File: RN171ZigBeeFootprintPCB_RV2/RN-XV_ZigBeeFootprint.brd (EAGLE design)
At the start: 39.1 x 52.1 mm, 20 parts

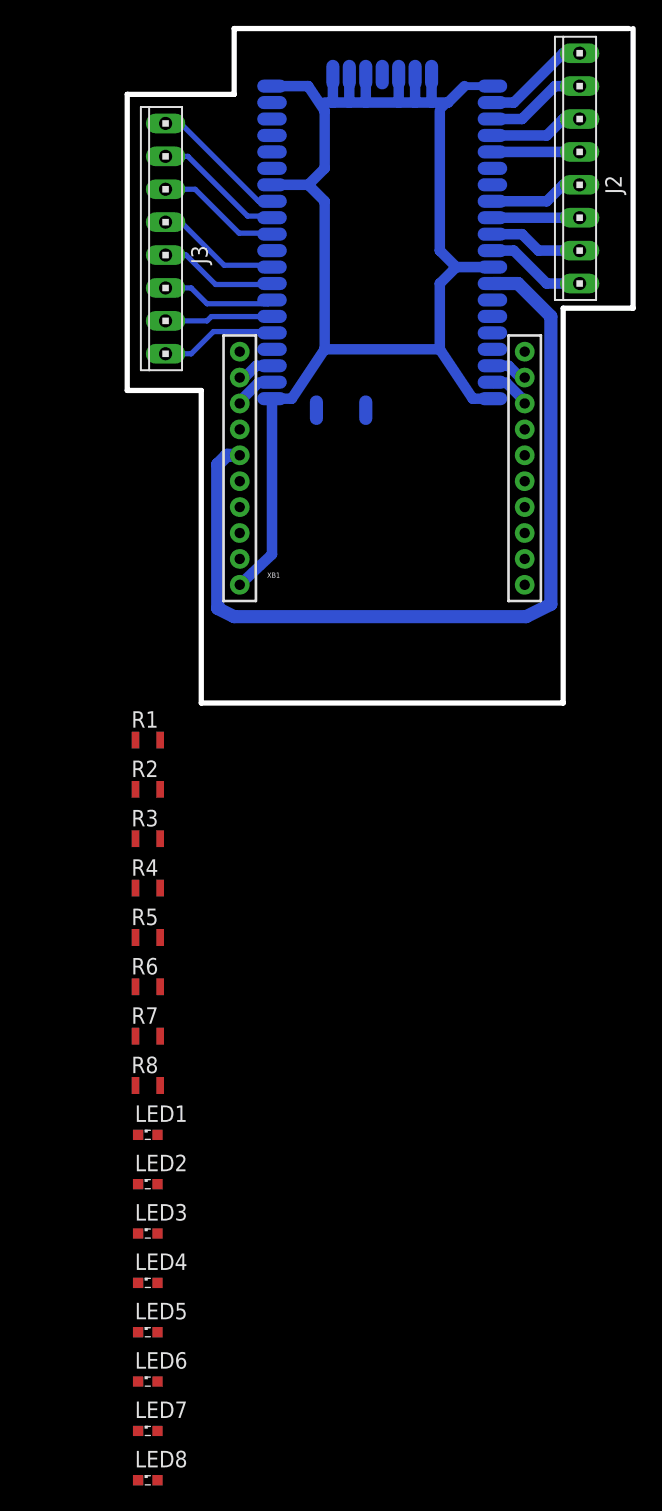
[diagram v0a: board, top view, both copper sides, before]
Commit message: Wired LED in to the PCB design.
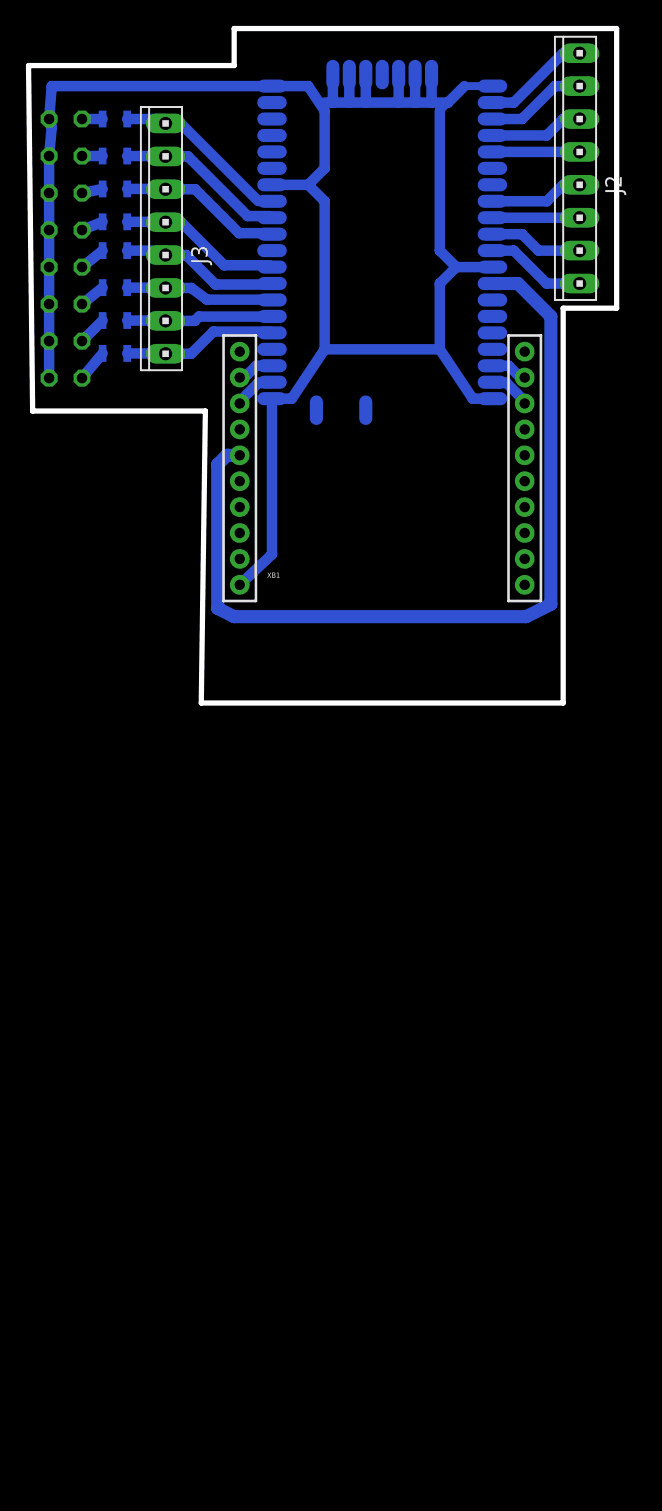
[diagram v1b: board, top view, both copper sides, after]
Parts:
- LED1, LED2, LED3, LED4, LED5, LED6, LED7, LED8: device eagle-ltspice:LED_SML0603 -> eagle-ltspice:LED_LD260
- moved LED8 105.3 mm to (-10.5, 39.7), flipped to the bottom
- moved LED7 98.6 mm to (-10.5, 36.8), flipped to the bottom
- moved LED6 92.0 mm to (-10.5, 34.0), flipped to the bottom
- moved LED5 85.3 mm to (-10.5, 31.1), flipped to the bottom
- moved LED4 78.7 mm to (-10.5, 28.3), flipped to the bottom
- moved R8 74.7 mm to (-6.67, 39.7), flipped to the bottom, turned to 180 degrees
- moved LED3 72.0 mm to (-10.5, 25.4), flipped to the bottom
- moved R7 68.0 mm to (-6.67, 36.8), flipped to the bottom, turned to 180 degrees
- moved LED2 65.4 mm to (-10.5, 22.5), flipped to the bottom
- moved R6 61.6 mm to (-6.67, 34.3), flipped to the bottom, turned to 180 degrees
- moved LED1 58.8 mm to (-10.5, 19.7), flipped to the bottom
- moved R5 55.3 mm to (-6.67, 31.8), flipped to the bottom, turned to 180 degrees
- moved R4 49.3 mm to (-6.67, 29.5), flipped to the bottom, turned to 180 degrees
- moved R3 42.6 mm to (-6.67, 26.7), flipped to the bottom, turned to 180 degrees
- moved R2 36.3 mm to (-6.67, 24.1), flipped to the bottom, turned to 180 degrees
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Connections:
- removed net N$12: J1.13, J3.1
- removed net N$13: J1.12, J3.2
- removed net N$14: J1.11, J3.3
- removed net N$15: J1.9, J3.4
- removed net N$16: J1.8, J3.5
- removed net N$17: J1.7, J3.6
- removed net N$18: J1.6, J3.7
- removed net N$19: J1.5, J3.8
- net GND: now also LED1.K, LED2.K, LED3.K, LED4.K, LED5.K, LED6.K, LED7.K, LED8.K; no longer LED1.C, LED2.C, LED3.C, LED4.C, LED5.C, LED6.C, LED7.C, LED8.C
- net N$30: now also J1.5, J3.8
- net N$31: now also J1.6, J3.7
- net N$32: now also J1.7, J3.6
- net N$33: now also J1.8, J3.5
- net N$34: now also J1.9, J3.4
- net N$35: now also J1.11, J3.3
- net N$36: now also J1.12, J3.2
- net N$37: now also J1.13, J3.1
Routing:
- net GND: track 114.1 -> 153.7 mm
- net N$37: track 0.00 -> 14.0 mm
- net N$36: track 0.00 -> 13.2 mm
- net N$35: track 0.00 -> 12.6 mm
- net N$34: track 0.00 -> 12.6 mm
- net N$33: track 0.00 -> 12.5 mm
- net N$30: track 0.00 -> 12.0 mm
- net N$32: track 0.00 -> 11.5 mm
- net N$31: track 0.00 -> 11.3 mm
- net N$12: track 10.7 -> 0.00 mm
- net N$13: track 10.2 -> 0.00 mm
- net N$14: track 9.65 -> 0.00 mm
- net N$15: track 9.65 -> 0.00 mm
- net N$16: track 9.19 -> 0.00 mm
- net N$19: track 8.97 -> 0.00 mm
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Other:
- board size 39.1 x 52.1 mm -> 45.4 x 52.1 mm
- board text added: "REV2.0"

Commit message: Connecting voltage supply to all components.
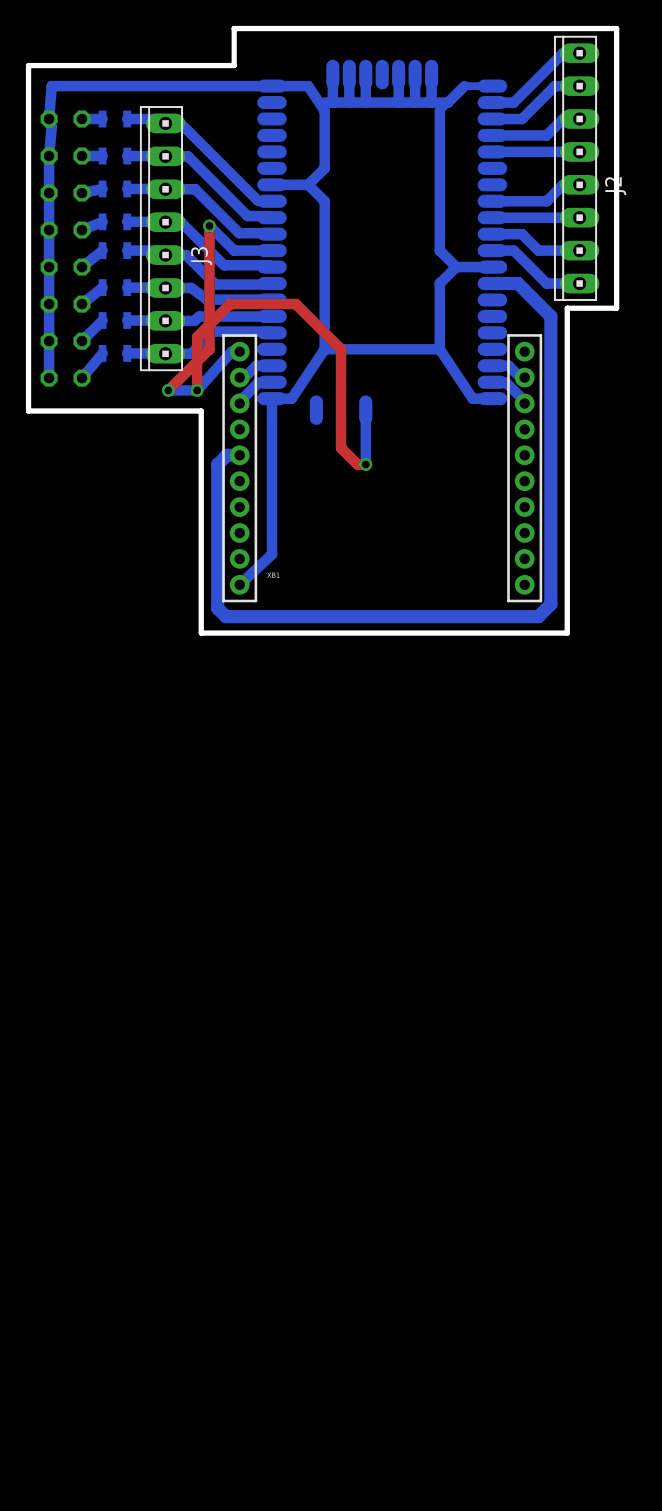
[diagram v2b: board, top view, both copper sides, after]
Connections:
- removed net VCC: XB1.1
- net VDD_3.3V: now also J1.49, XB1.1
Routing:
- net VDD_3.3V: track 0.00 -> 58.5 mm, vias 0 -> 4
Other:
- board size 45.4 x 52.1 mm -> 45.4 x 46.7 mm
- board text added: "GND"
- board text added: "REV 2.0"
- board text removed: "REV2.0"
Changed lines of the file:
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@@
 <layer number="36" name="bGlue" color="7" fill="5" visible="no" active="yes"/>
 <layer number="37" name="tTest" color="7" fill="1" visible="no" active="yes"/>
-<layer number="38" name="bTest" color="7" fill="1" visible="no" active="yes"/>
+<layer number="38" name="bTest" color="7" fill="1" visible="yes" active="yes"/>
 <layer number="39" name="tKeepout" color="4" fill="11" visible="yes" active="yes"/>
 <layer number="40" name="bKeepout" color="1" fill="11" visible="yes" active="yes"/>
@@
 <board>
 <plain>
-<wire x1="-13.335" y1="43.815" x2="-13.0175" y2="17.145" width="0.4064" layer="46"/>
-<wire x1="-13.0175" y1="17.145" x2="0.3175" y2="17.145" width="0.4064" layer="46"/>
-<wire x1="0.3175" y1="17.145" x2="0" y2="-5.3975" width="0.4064" layer="46"/>
-<wire x1="0" y1="-5.3975" x2="27.94" y2="-5.3975" width="0.4064" layer="46"/>
-<wire x1="27.94" y1="-5.3975" x2="27.94" y2="25.0825" width="0.4064" layer="46"/>
-<wire x1="27.94" y1="25.0825" x2="32.0675" y2="25.0825" width="0.4064" layer="46"/>
+<wire x1="-13.335" y1="43.815" x2="-13.335" y2="17.145" width="0.4064" layer="46"/>
+<wire x1="-13.335" y1="17.145" x2="0" y2="17.145" width="0.4064" layer="46"/>
+<wire x1="0" y1="17.145" x2="0" y2="0" width="0.4064" layer="46"/>
+<wire x1="0" y1="0" x2="28.2575" y2="0" width="0.4064" layer="46"/>
+<wire x1="28.2575" y1="0" x2="28.2575" y2="25.0825" width="0.4064" layer="46"/>
+<wire x1="28.2575" y1="25.0825" x2="32.0675" y2="25.0825" width="0.4064" layer="46"/>
 <wire x1="32.0675" y1="25.0825" x2="32.0675" y2="46.6725" width="0.4064" layer="46"/>
 <wire x1="32.0675" y1="46.6725" x2="2.54" y2="46.6725" width="0.4064" layer="46"/>
 <wire x1="2.54" y1="46.6725" x2="2.54" y2="43.815" width="0.4064" layer="46"/>
 <wire x1="2.54" y1="43.815" x2="-13.335" y2="43.815" width="0.4064" layer="46"/>
-<text x="17.4625" y="-3.81" size="1.778" layer="48">REV2.0</text>
+<text x="9.8425" y="2.8575" size="1.778" layer="48">REV 2.0</text>
+<text x="16.51" y="38.1" size="1.778" layer="38" rot="MR0">GND</text>
+<text x="12.065" y="28.8925" size="1.778" layer="38" rot="MR270">GND</text>
+<text x="15.875" y="28.575" size="1.778" layer="38" rot="MR90">GND</text>
 </plain>
 <attributes>
@@
 <wire x1="1.9797" y1="13.7272" x2="1.27" y2="13.0175" width="1.016" layer="16"/>
 <wire x1="1.27" y1="13.0175" x2="1.27" y2="1.905" width="1.016" layer="16"/>
-<wire x1="1.27" y1="1.905" x2="2.54" y2="1.27" width="1.016" layer="16"/>
-<wire x1="2.54" y1="1.27" x2="25.0825" y2="1.27" width="1.016" layer="16"/>
-<wire x1="25.0825" y1="1.27" x2="26.9875" y2="2.2225" width="1.016" layer="16"/>
+<wire x1="1.27" y1="1.905" x2="1.905" y2="1.27" width="1.016" layer="16"/>
+<wire x1="1.905" y1="1.27" x2="26.035" y2="1.27" width="1.016" layer="16"/>
+<wire x1="26.035" y1="1.27" x2="26.9875" y2="2.2225" width="1.016" layer="16"/>
 <wire x1="26.9875" y1="2.2225" x2="26.9875" y2="24.4475" width="1.016" layer="16"/>
 <wire x1="26.9875" y1="24.4475" x2="24.4475" y2="26.9875" width="1.016" layer="16"/>
@@
 <wire x1="2.97" y1="17.8798" x2="2.97" y2="17.7272" width="0.8128" layer="16"/>
 </signal>
-<signal name="VCC">
-<contactref element="XB1" pad="1"/>
-</signal>
 <signal name="VDD_3.3V">
 <contactref element="J1" pad="10"/>
+<contactref element="J1" pad="49"/>
+<contactref element="XB1" pad="1"/>
+<wire x1="2.97" y1="21.7272" x2="2.3597" y2="21.7272" width="0.8128" layer="16"/>
+<wire x1="2.3597" y1="21.7272" x2="-0.3175" y2="18.7325" width="0.8128" layer="16"/>
+<via x="-0.3175" y="18.7325" extent="1-16" drill="0.6" shape="square"/>
+<wire x1="-0.3175" y1="18.7325" x2="-0.3175" y2="22.86" width="0.8128" layer="1"/>
+<wire x1="-0.3175" y1="22.86" x2="2.2225" y2="25.4" width="0.8128" layer="1"/>
+<wire x1="2.2225" y1="25.4" x2="7.3025" y2="25.4" width="0.8128" layer="1"/>
+<wire x1="7.3025" y1="25.4" x2="10.795" y2="21.9075" width="0.8128" layer="1"/>
+<wire x1="10.795" y1="21.9075" x2="10.795" y2="14.2875" width="0.8128" layer="1"/>
+<wire x1="10.795" y1="14.2875" x2="12.065" y2="13.0175" width="0.8128" layer="1"/>
+<wire x1="12.065" y1="13.0175" x2="12.7" y2="13.0175" width="0.8128" layer="1"/>
+<via x="12.7" y="13.0175" extent="1-16" drill="0.6" shape="square"/>
+<wire x1="12.7" y1="13.0175" x2="12.7" y2="17.2085" width="0.8128" layer="16"/>
+<wire x1="5.461" y1="29.5275" x2="2.54" y2="29.5275" width="0.8128" layer="16"/>
+<wire x1="2.54" y1="29.5275" x2="0.635" y2="31.4325" width="0.8128" layer="16"/>
+<via x="0.635" y="31.4325" extent="1-16" drill="0.6" shape="square"/>
+<wire x1="0.635" y1="31.4325" x2="0.635" y2="21.9075" width="0.8128" layer="1"/>
+<wire x1="0.635" y1="21.9075" x2="-2.54" y2="18.7325" width="0.8128" layer="1"/>
+<via x="-2.54" y="18.7325" extent="1-16" drill="0.6" shape="square"/>
+<wire x1="-2.54" y1="18.7325" x2="-0.3175" y2="18.7325" width="0.8128" layer="16"/>
 </signal>
 <signal name="N$1">

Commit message: Connecting RN171's 34 pin to VCC
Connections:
- net VDD_3.3V: now also J1.34
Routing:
- net VDD_3.3V: track 58.5 -> 98.2 mm, vias 4 -> 6
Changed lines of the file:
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@@
 <via x="-2.54" y="18.7325" extent="1-16" drill="0.6" shape="square"/>
 <wire x1="-2.54" y1="18.7325" x2="-0.3175" y2="18.7325" width="0.8128" layer="16"/>
+<contactref element="J1" pad="34"/>
+<wire x1="22.479" y1="34.6075" x2="25.7175" y2="34.6075" width="0.8128" layer="16"/>
+<wire x1="25.7175" y1="34.6075" x2="25.7175" y2="35.56" width="0.8128" layer="16"/>
+<via x="25.7175" y="35.56" extent="1-16" drill="0.6" shape="square"/>
+<wire x1="25.7175" y1="35.56" x2="15.875" y2="35.56" width="0.8128" layer="1"/>
+<wire x1="15.875" y1="35.56" x2="15.875" y2="13.0175" width="0.8128" layer="1"/>
+<via x="15.875" y="13.0175" extent="1-16" drill="0.6" shape="square"/>
+<wire x1="15.875" y1="13.0175" x2="12.7" y2="13.0175" width="0.8128" layer="16"/>
 </signal>
 <signal name="N$1">

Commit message: Replace one of the line in the PCB design.
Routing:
- net VDD_3.3V: track 98.2 -> 92.8 mm, vias 6 -> 4
- net GND: track 153.7 -> 155.0 mm
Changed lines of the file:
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@@
 <wire x1="22.479" y1="28.2575" x2="19.685" y2="28.2575" width="0.8128" layer="16"/>
 <wire x1="19.685" y1="28.2575" x2="18.415" y2="26.9875" width="0.8128" layer="16"/>
-<wire x1="18.415" y1="26.9875" x2="18.415" y2="21.9075" width="0.8128" layer="16"/>
-<wire x1="18.415" y1="21.9075" x2="20.955" y2="18.0975" width="0.8128" layer="16"/>
+<wire x1="18.415" y1="26.9875" x2="18.415" y2="20.6375" width="0.8128" layer="16"/>
 <wire x1="20.955" y1="18.0975" x2="22.479" y2="18.0975" width="0.8128" layer="16"/>
 <contactref element="J1" pad="27"/>
@@
 <wire x1="16.51" y1="43.1165" x2="16.51" y2="40.9575" width="0.8128" layer="16"/>
 <wire x1="17.78" y1="43.1165" x2="17.78" y2="40.9575" width="0.8128" layer="16"/>
-<wire x1="18.415" y1="21.9075" x2="9.525" y2="21.9075" width="0.8128" layer="16"/>
-<wire x1="9.525" y1="21.9075" x2="6.985" y2="18.0975" width="0.8128" layer="16"/>
 <wire x1="6.985" y1="18.0975" x2="5.461" y2="18.0975" width="0.8128" layer="16"/>
-<wire x1="8.255" y1="34.6075" x2="9.525" y2="33.3375" width="0.8128" layer="16"/>
-<wire x1="9.525" y1="33.3375" x2="9.525" y2="21.9075" width="0.8128" layer="16"/>
+<wire x1="8.255" y1="34.6075" x2="9.525" y2="33.3375" width="0" layer="19" extent="1-16"/>
+<wire x1="9.525" y1="33.3375" x2="9.525" y2="21.9075" width="0" layer="19" extent="1-16"/>
 <wire x1="2.97" y1="3.7272" x2="5.461" y2="6.0785" width="0.8128" layer="16"/>
 <contactref element="LED8" pad="K"/>
@@
 <wire x1="5.461" y1="42.2275" x2="-11.545" y2="42.2275" width="0.8128" layer="16"/>
 <wire x1="-11.545" y1="42.2275" x2="-11.7475" y2="39.6875" width="0.8128" layer="16"/>
+<wire x1="6.985" y1="18.0975" x2="6.985" y2="11.43" width="0.8128" layer="16"/>
+<wire x1="6.985" y1="11.43" x2="7.9375" y2="10.795" width="0.8128" layer="16"/>
+<wire x1="7.9375" y1="10.795" x2="20.0025" y2="10.795" width="0.8128" layer="16"/>
+<wire x1="20.0025" y1="10.795" x2="20.955" y2="11.43" width="0.8128" layer="16"/>
+<wire x1="20.955" y1="11.43" x2="20.955" y2="18.0975" width="0.8128" layer="16"/>
+<wire x1="18.415" y1="20.6375" x2="20.955" y2="18.0975" width="0.8128" layer="16"/>
 </signal>
 <signal name="RX">
@@
 <via x="12.7" y="13.0175" extent="1-16" drill="0.6" shape="square"/>
 <wire x1="12.7" y1="13.0175" x2="12.7" y2="17.2085" width="0.8128" layer="16"/>
-<wire x1="5.461" y1="29.5275" x2="2.54" y2="29.5275" width="0.8128" layer="16"/>
-<wire x1="2.54" y1="29.5275" x2="0.635" y2="31.4325" width="0.8128" layer="16"/>
-<via x="0.635" y="31.4325" extent="1-16" drill="0.6" shape="square"/>
-<wire x1="0.635" y1="31.4325" x2="0.635" y2="21.9075" width="0.8128" layer="1"/>
-<wire x1="0.635" y1="21.9075" x2="-2.54" y2="18.7325" width="0.8128" layer="1"/>
-<via x="-2.54" y="18.7325" extent="1-16" drill="0.6" shape="square"/>
-<wire x1="-2.54" y1="18.7325" x2="-0.3175" y2="18.7325" width="0.8128" layer="16"/>
 <contactref element="J1" pad="34"/>
 <wire x1="22.479" y1="34.6075" x2="25.7175" y2="34.6075" width="0.8128" layer="16"/>
@@
 <via x="15.875" y="13.0175" extent="1-16" drill="0.6" shape="square"/>
 <wire x1="15.875" y1="13.0175" x2="12.7" y2="13.0175" width="0.8128" layer="16"/>
+<wire x1="5.461" y1="29.5275" x2="7.3025" y2="29.5275" width="0.8128" layer="16"/>
+<wire x1="7.3025" y1="29.5275" x2="12.7" y2="24.13" width="0.8128" layer="16"/>
+<wire x1="12.7" y1="24.13" x2="12.7" y2="17.2085" width="0.8128" layer="16"/>
 </signal>
 <signal name="N$1">
